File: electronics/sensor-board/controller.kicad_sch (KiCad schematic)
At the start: 21 parts, among them SW5 SW_Push, SW6 SW_Push, U9 STM32F302C8Tx, Y1 8MHz

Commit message: Update reference designators
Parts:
- renumbered R41 to R33, R42 to R34, R43 to R35, R44 to R36, R45 to R37, SW5 to SW1, SW6 to SW2
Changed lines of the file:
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@@
   (symbol (lib_id "power:+3.3V") (at 121.92 58.42 0) (unit 1)
     (in_bom yes) (on_board yes) (fields_autoplaced)
-    (property "Reference" "#PWR077" (id 0) (at 121.92 62.23 0)
+    (property "Reference" "#PWR075" (id 0) (at 121.92 62.23 0)
       (effects (font (size 1.27 1.27)) hide)
     )
@@
   (symbol (lib_id "power:+3.3V") (at 81.28 64.77 0) (unit 1)
     (in_bom yes) (on_board yes) (fields_autoplaced)
-    (property "Reference" "#PWR076" (id 0) (at 81.28 68.58 0)
+    (property "Reference" "#PWR074" (id 0) (at 81.28 68.58 0)
       (effects (font (size 1.27 1.27)) hide)
     )
@@
   (symbol (lib_id "power:GND") (at 124.46 139.7 0) (unit 1)
     (in_bom yes) (on_board yes) (fields_autoplaced)
-    (property "Reference" "#PWR078" (id 0) (at 124.46 146.05 0)
+    (property "Reference" "#PWR076" (id 0) (at 124.46 146.05 0)
       (effects (font (size 1.27 1.27)) hide)
     )
@@
   (symbol (lib_id "power:GND") (at 149.86 83.82 0) (unit 1)
     (in_bom yes) (on_board yes) (fields_autoplaced)
-    (property "Reference" "#PWR083" (id 0) (at 149.86 90.17 0)
+    (property "Reference" "#PWR081" (id 0) (at 149.86 90.17 0)
       (effects (font (size 1.27 1.27)) hide)
     )
@@
   (symbol (lib_id "power:GND") (at 149.86 60.96 0) (unit 1)
     (in_bom yes) (on_board yes) (fields_autoplaced)
-    (property "Reference" "#PWR081" (id 0) (at 149.86 67.31 0)
+    (property "Reference" "#PWR079" (id 0) (at 149.86 67.31 0)
       (effects (font (size 1.27 1.27)) hide)
     )
@@
   (symbol (lib_id "power:+3.3VA") (at 149.86 50.8 0) (unit 1)
     (in_bom yes) (on_board yes) (fields_autoplaced)
-    (property "Reference" "#PWR080" (id 0) (at 149.86 54.61 0)
+    (property "Reference" "#PWR078" (id 0) (at 149.86 54.61 0)
       (effects (font (size 1.27 1.27)) hide)
     )
@@
   (symbol (lib_id "power:+3.3VA") (at 132.08 58.42 0) (unit 1)
     (in_bom yes) (on_board yes) (fields_autoplaced)
-    (property "Reference" "#PWR079" (id 0) (at 132.08 62.23 0)
+    (property "Reference" "#PWR077" (id 0) (at 132.08 62.23 0)
       (effects (font (size 1.27 1.27)) hide)
     )
@@
   (symbol (lib_id "power:+3.3V") (at 149.86 73.66 0) (unit 1)
     (in_bom yes) (on_board yes) (fields_autoplaced)
-    (property "Reference" "#PWR082" (id 0) (at 149.86 77.47 0)
+    (property "Reference" "#PWR080" (id 0) (at 149.86 77.47 0)
       (effects (font (size 1.27 1.27)) hide)
     )
@@
   (symbol (lib_id "Device:R_Small") (at 86.36 69.85 90) (unit 1)
     (in_bom yes) (on_board yes)
-    (property "Reference" "R41" (id 0) (at 92.71 68.58 90)
+    (property "Reference" "R33" (id 0) (at 92.71 68.58 90)
       (effects (font (size 1.27 1.27)) (justify left))
     )
@@
   (symbol (lib_id "Device:R_Small") (at 101.6 83.82 90) (unit 1)
     (in_bom yes) (on_board yes)
-    (property "Reference" "R42" (id 0) (at 107.95 82.55 90)
+    (property "Reference" "R34" (id 0) (at 107.95 82.55 90)
       (effects (font (size 1.27 1.27)) (justify left))
     )
@@
   (symbol (lib_id "Device:R_Small") (at 101.6 86.36 90) (unit 1)
     (in_bom yes) (on_board yes)
-    (property "Reference" "R43" (id 0) (at 107.95 85.09 90)
+    (property "Reference" "R35" (id 0) (at 107.95 85.09 90)
       (effects (font (size 1.27 1.27)) (justify left))
     )
@@
   (symbol (lib_id "Switch:SW_Push") (at 90.17 55.88 0) (unit 1)
     (in_bom yes) (on_board yes)
-    (property "Reference" "SW5" (id 0) (at 95.25 53.34 0))
+    (property "Reference" "SW1" (id 0) (at 95.25 53.34 0))
     (property "Value" "SW_Push" (id 1) (at 82.55 53.34 0)
       (effects (font (size 1.27 1.27)) hide)
@@
   (symbol (lib_id "Device:R_Small") (at 101.6 88.9 90) (unit 1)
     (in_bom yes) (on_board yes)
-    (property "Reference" "R44" (id 0) (at 107.95 87.63 90)
+    (property "Reference" "R36" (id 0) (at 107.95 87.63 90)
       (effects (font (size 1.27 1.27)) (justify left))
     )
@@
   (symbol (lib_id "power:GND") (at 77.47 91.44 0) (unit 1)
     (in_bom yes) (on_board yes) (fields_autoplaced)
-    (property "Reference" "#PWR075" (id 0) (at 77.47 97.79 0)
+    (property "Reference" "#PWR073" (id 0) (at 77.47 97.79 0)
       (effects (font (size 1.27 1.27)) hide)
     )
@@
   (symbol (lib_id "Switch:SW_Push") (at 90.17 66.04 0) (unit 1)
     (in_bom yes) (on_board yes)
-    (property "Reference" "SW6" (id 0) (at 95.25 63.5 0))
+    (property "Reference" "SW2" (id 0) (at 95.25 63.5 0))
     (property "Value" "SW_Push" (id 1) (at 82.55 63.5 0)
       (effects (font (size 1.27 1.27)) hide)
@@
   (symbol (lib_id "Device:R_Small") (at 102.87 78.74 90) (unit 1)
     (in_bom yes) (on_board yes)
-    (property "Reference" "R45" (id 0) (at 109.22 77.47 90)
-      (effects (font (size 1.27 1.27)) (justify left))
-    )
+    (property "Reference" "R37" (id 0) (at 109.22 77.47 90)
+      (effects (font (size 1.27 1.27)) (justify left))
+    )

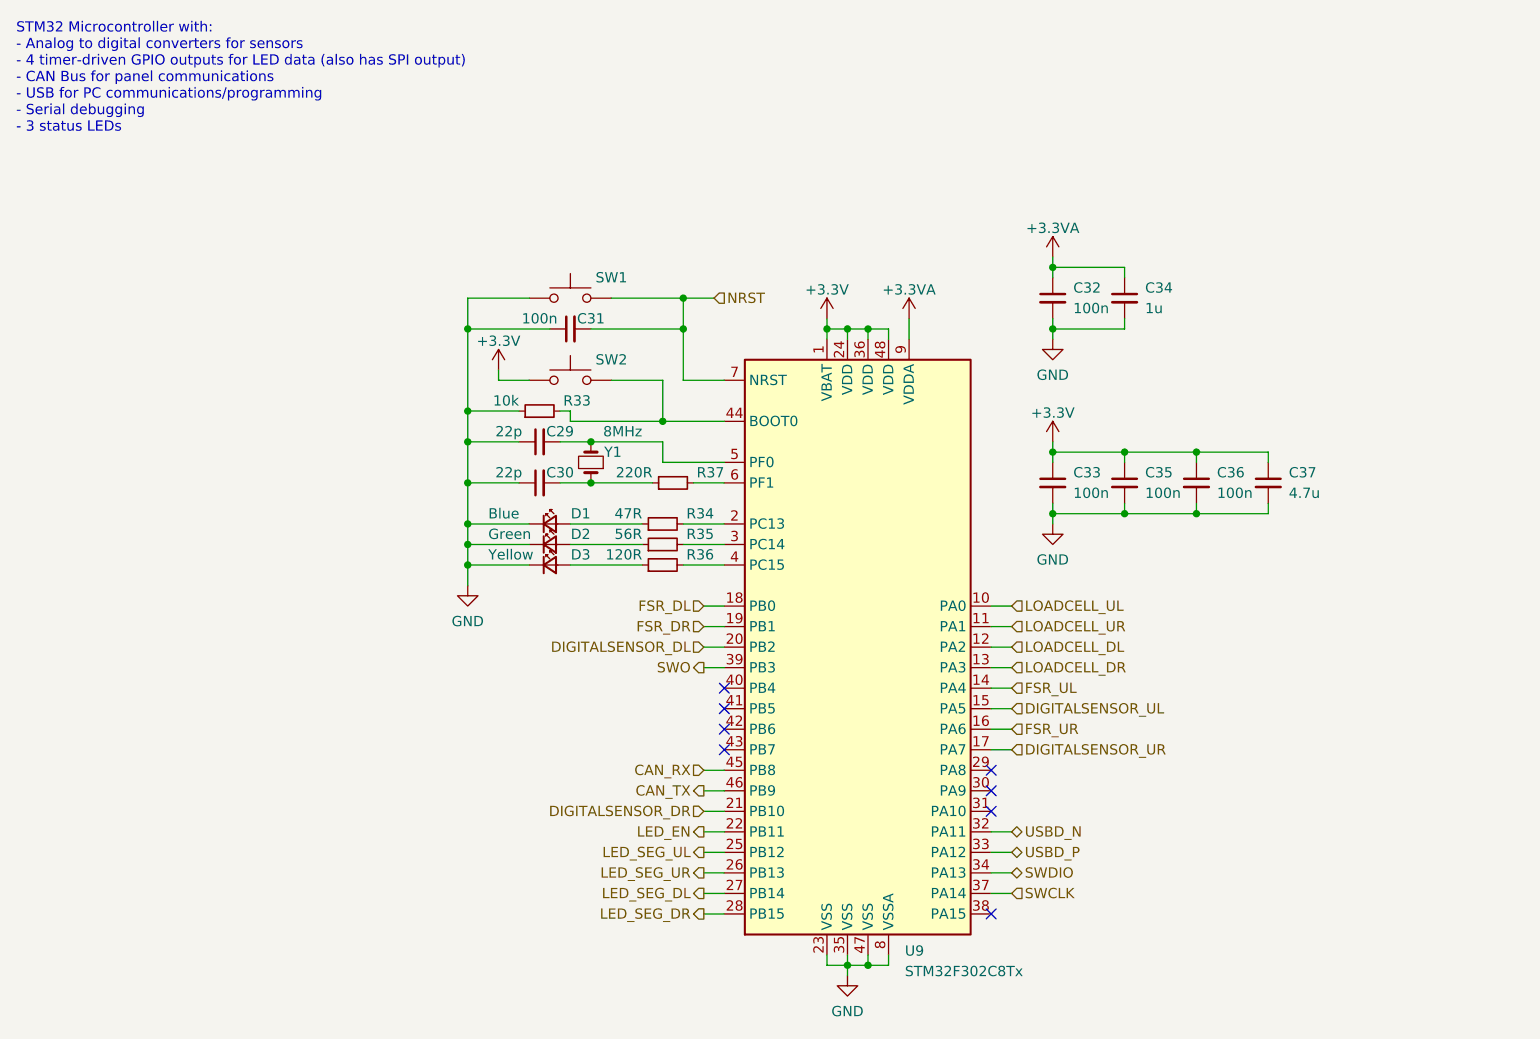
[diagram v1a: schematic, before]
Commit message: Upgrade to STM32G4 and CAN FD
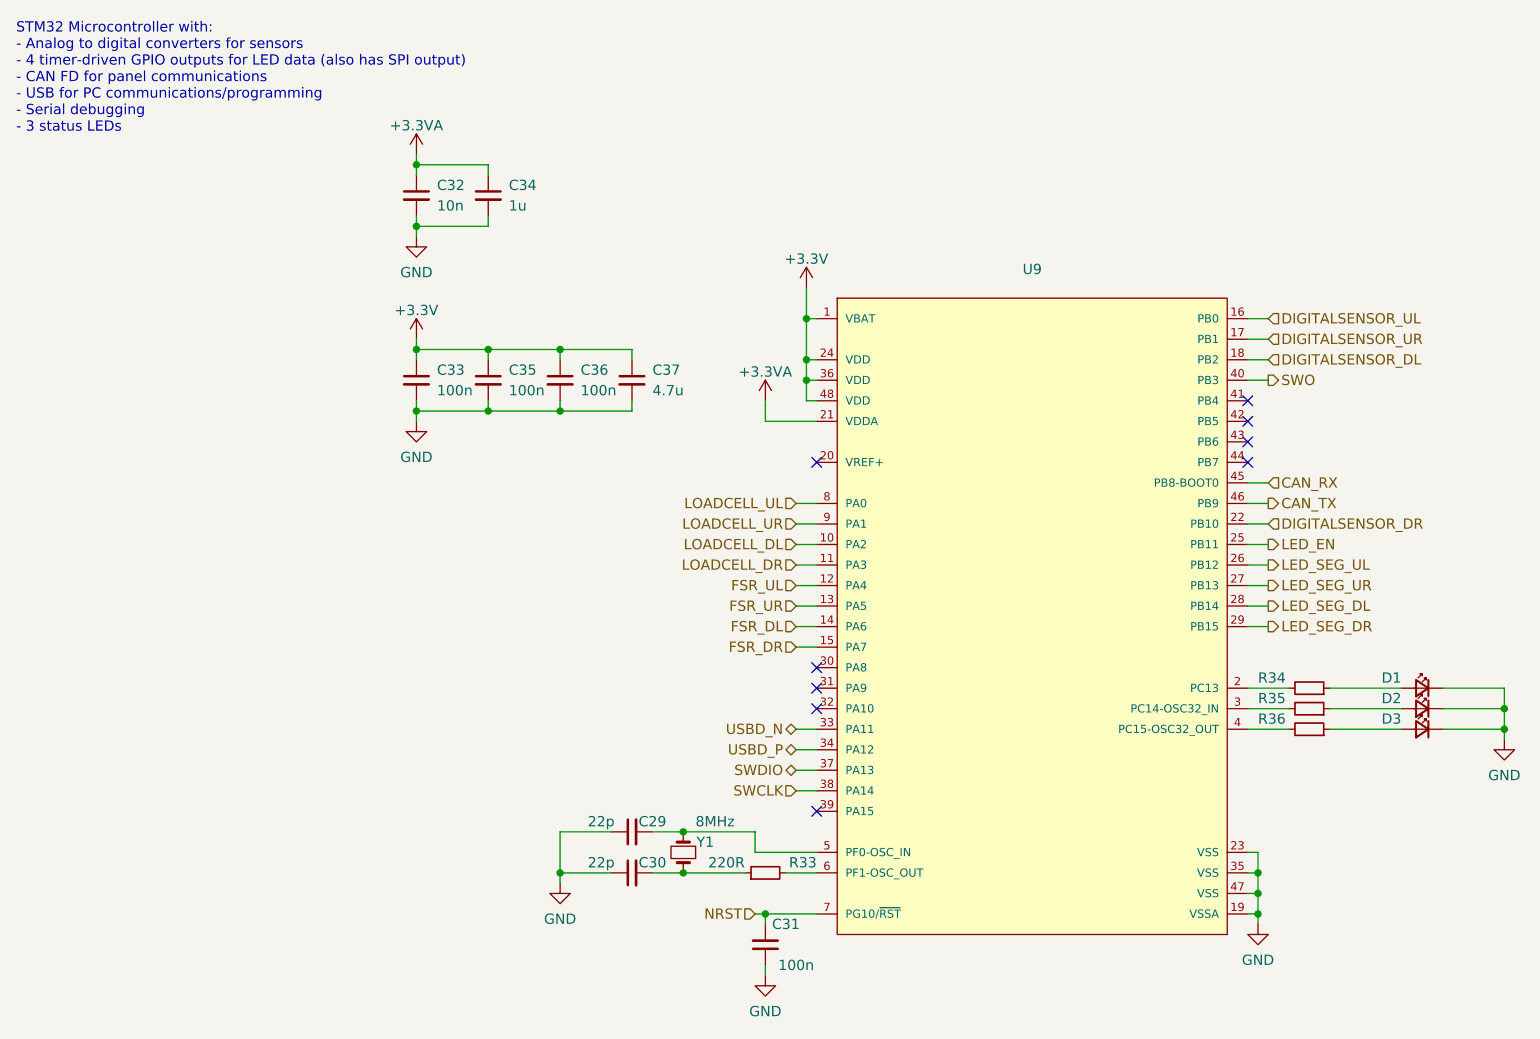
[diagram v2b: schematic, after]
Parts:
- removed R37: 220R, Resistor_SMD:R_0603_1608Metric, symbol Device:R_Small
- removed SW1, SW2: SW_Push, sensor-board:TS-1187A-B-A-B, symbol Switch:SW_Push
- removed U9: STM32F302C8Tx, Package_QFP:LQFP-48_7x7mm_P0.5mm, symbol MCU_ST_STM32F3:STM32F302C8Tx
- added U9: (no value), Package_QFP:LQFP-48_7x7mm_P0.5mm, symbol MCU:STM32G431CBT6
- C32: value 100n -> 10n
- D1: value Blue -> (none); footprint LED_SMD:LED_0603_1608Metric -> (none)
- D2: value Green -> (none); footprint LED_SMD:LED_0603_1608Metric -> (none)
- D3: value Yellow -> (none); footprint LED_SMD:LED_0603_1608Metric -> (none)
- R33: value 10k -> 220R
- R34: value 47R -> (none); footprint Resistor_SMD:R_0603_1608Metric -> (none)
- R35: value 56R -> (none); footprint Resistor_SMD:R_0603_1608Metric -> (none)
- R36: value 120R -> (none); footprint Resistor_SMD:R_0603_1608Metric -> (none)
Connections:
- net +3.3V: now also U9.1 (VBAT), U9.24 (VDD), U9.36 (VDD), U9.48 (VDD)
- net +3.3VA: now also U9.21 (VDDA)
- net CAN_RX: now also U9.45 (PB8-BOOT0)
- net CAN_TX: now also U9.46 (PB9)
- net DIGITALSENSOR_DL: now also U9.18 (PB2)
- net DIGITALSENSOR_DR: now also U9.22 (PB10)
- net DIGITALSENSOR_UL: now also U9.16 (PB0)
- net DIGITALSENSOR_UR: now also U9.17 (PB1)
- net FSR_DL: now also U9.14 (PA6)
- net FSR_DR: now also U9.15 (PA7)
- net FSR_UL: now also U9.12 (PA4)
- net FSR_UR: now also U9.13 (PA5)
- net GND: now also U9.19 (VSSA), U9.23 (VSS), U9.35 (VSS), U9.47 (VSS); no longer R33.1
- net LED_EN: now also U9.25 (PB11)
- net LED_SEG_DL: now also U9.28 (PB14)
- net LED_SEG_DR: now also U9.29 (PB15)
- net LED_SEG_UL: now also U9.26 (PB12)
- net LED_SEG_UR: now also U9.27 (PB13)
- net LOADCELL_DL: now also U9.10 (PA2)
- net LOADCELL_DR: now also U9.11 (PA3)
- net LOADCELL_UL: now also U9.8 (PA0)
- net LOADCELL_UR: now also U9.9 (PA1)
- net NRST: now also U9.7 (PG10/~{RST})
- net SWCLK: now also U9.38 (PA14)
- net SWDIO: now also U9.37 (PA13)
- net SWO: now also U9.40 (PB3)
- net USBD_N: now also U9.33 (PA11)
- net USBD_P: now also U9.34 (PA12)
- net at C29.2, Y1.2: now also U9.5 (PF0-OSC_IN)
- net at C30.2, Y1.1: now also R33.1
- net at R33.2: now also U9.6 (PF1-OSC_OUT)
- net at R34.2: now also U9.2 (PC13)
- net at R35.2: now also U9.3 (PC14-OSC32_IN)
- net at R36.2: now also U9.4 (PC15-OSC32_OUT)
- no-connect marks 8 -> 9
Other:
- note added: "STM32 Microcontroller with: - Analog to digital converters for sensors - 4 timer-driven GPIO outputs for LED data (also has SPI output) - CAN FD for panel communications - USB for PC communications/programming - Serial debugging - 3 status LEDs"
- note removed: "STM32 Microcontroller with: - Analog to digital converters for sensors - 4 timer-driven GPIO outputs for LED data (also has SPI output) - CAN Bus for panel communications - USB for PC communications/programming - Serial debugging - 3 status LEDs"
- moved on the sheet: C32, C33, C34, C35, C36, C37

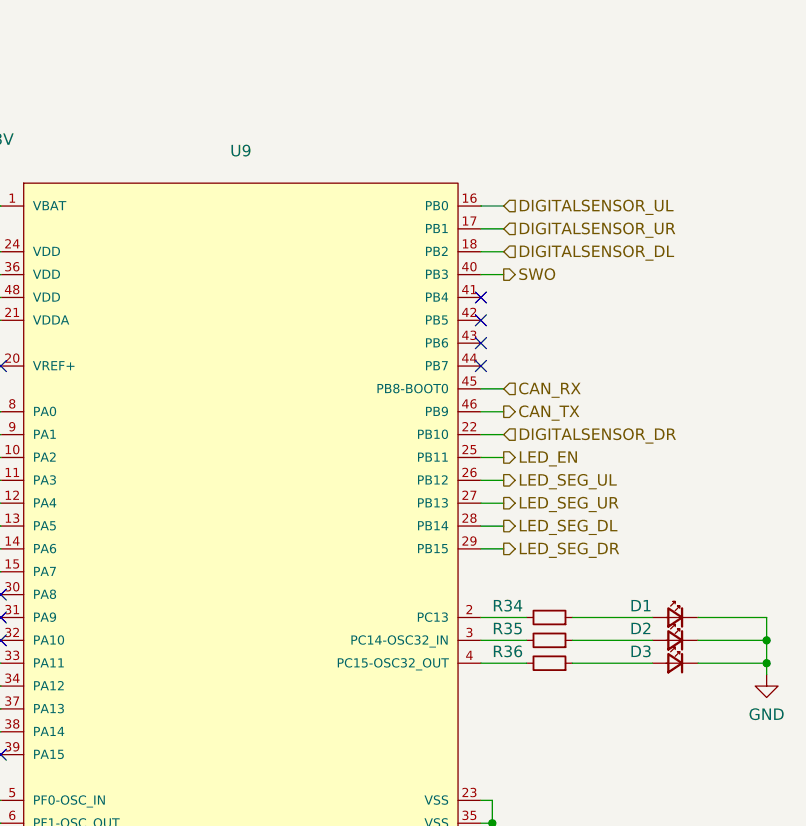
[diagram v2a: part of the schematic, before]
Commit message: Switch to G4, preliminary signal layout
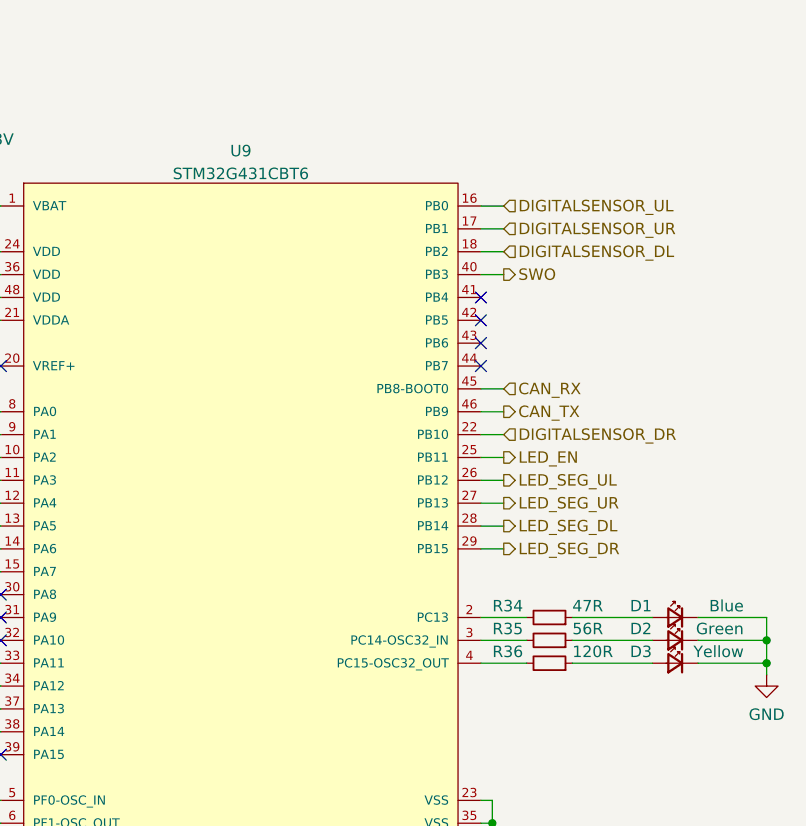
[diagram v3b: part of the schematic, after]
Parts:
- D1: value (none) -> Blue; footprint (none) -> LED_SMD:LED_0603_1608Metric
- D2: value (none) -> Green; footprint (none) -> LED_SMD:LED_0603_1608Metric
- D3: value (none) -> Yellow; footprint (none) -> LED_SMD:LED_0603_1608Metric
- R34: value (none) -> 47R; footprint (none) -> Resistor_SMD:R_0603_1608Metric
- R35: value (none) -> 56R; footprint (none) -> Resistor_SMD:R_0603_1608Metric
- R36: value (none) -> 120R; footprint (none) -> Resistor_SMD:R_0603_1608Metric
- U9: value (none) -> STM32G431CBT6
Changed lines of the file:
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@@
     (in_bom yes) (on_board yes) (fields_autoplaced)
     (property "Reference" "U9" (id 0) (at 147.32 52.3072 0))
-    (property "Value" "" (id 1) (at 147.32 54.8441 0))
+    (property "Value" "STM32G431CBT6" (id 1) (at 147.32 54.8441 0))
     (property "Footprint" "Package_QFP:LQFP-48_7x7mm_P0.5mm" (id 2) (at 118.11 48.26 0)
       (effects (font (size 1.27 1.27)) (justify left) hide)
@@
       (effects (font (size 1.27 1.27)) (justify left))
     )
-    (property "Value" "" (id 1) (at 184.15 102.87 90)
-      (effects (font (size 1.27 1.27)) (justify left))
-    )
-    (property "Footprint" "" (id 2) (at 181.61 104.14 0)
+    (property "Value" "47R" (id 1) (at 184.15 102.87 90)
+      (effects (font (size 1.27 1.27)) (justify left))
+    )
+    (property "Footprint" "Resistor_SMD:R_0603_1608Metric" (id 2) (at 181.61 104.14 0)
       (effects (font (size 1.27 1.27)) hide)
     )
@@
       (effects (font (size 1.27 1.27)) (justify left))
     )
-    (property "Value" "" (id 1) (at 184.15 107.95 90)
-      (effects (font (size 1.27 1.27)) (justify left))
-    )
-    (property "Footprint" "" (id 2) (at 181.61 109.22 0)
+    (property "Value" "120R" (id 1) (at 184.15 107.95 90)
+      (effects (font (size 1.27 1.27)) (justify left))
+    )
+    (property "Footprint" "Resistor_SMD:R_0603_1608Metric" (id 2) (at 181.61 109.22 0)
       (effects (font (size 1.27 1.27)) hide)
     )
@@
     (in_bom yes) (on_board yes)
     (property "Reference" "D1" (id 0) (at 191.77 102.87 0))
-    (property "Value" "" (id 1) (at 203.2 102.87 0)
-      (effects (font (size 1.27 1.27)) (justify left))
-    )
-    (property "Footprint" "" (id 2) (at 195.58 104.14 90)
+    (property "Value" "Blue" (id 1) (at 203.2 102.87 0)
+      (effects (font (size 1.27 1.27)) (justify left))
+    )
+    (property "Footprint" "LED_SMD:LED_0603_1608Metric" (id 2) (at 195.58 104.14 90)
       (effects (font (size 1.27 1.27)) hide)
     )
@@
     (in_bom yes) (on_board yes)
     (property "Reference" "D3" (id 0) (at 191.77 107.95 0))
-    (property "Value" "" (id 1) (at 203.2 107.95 0)
-      (effects (font (size 1.27 1.27)) (justify left))
-    )
-    (property "Footprint" "" (id 2) (at 195.58 109.22 90)
+    (property "Value" "Yellow" (id 1) (at 203.2 107.95 0)
+      (effects (font (size 1.27 1.27)) (justify left))
+    )
+    (property "Footprint" "LED_SMD:LED_0603_1608Metric" (id 2) (at 195.58 109.22 90)
       (effects (font (size 1.27 1.27)) hide)
     )
@@
       (effects (font (size 1.27 1.27)) (justify left))
     )
-    (property "Value" "" (id 1) (at 184.15 105.41 90)
-      (effects (font (size 1.27 1.27)) (justify left))
-    )
-    (property "Footprint" "" (id 2) (at 181.61 106.68 0)
+    (property "Value" "56R" (id 1) (at 184.15 105.41 90)
+      (effects (font (size 1.27 1.27)) (justify left))
+    )
+    (property "Footprint" "Resistor_SMD:R_0603_1608Metric" (id 2) (at 181.61 106.68 0)
       (effects (font (size 1.27 1.27)) hide)
     )
@@
     (in_bom yes) (on_board yes)
     (property "Reference" "D2" (id 0) (at 191.77 105.41 0))
-    (property "Value" "" (id 1) (at 203.2 105.41 0)
-      (effects (font (size 1.27 1.27)) (justify left))
-    )
-    (property "Footprint" "" (id 2) (at 195.58 106.68 90)
-      (effects (font (size 1.27 1.27)) hide)
-    )
+    (property "Value" "Green" (id 1) (at 203.2 105.41 0)
+      (effects (font (size 1.27 1.27)) (justify left))
+    )
+    (property "Footprint" "LED_SMD:LED_0603_1608Metric" (id 2) (at 195.58 106.68 90)
+      (effects (font (size 1.27 1.27)) hide)
+    )
